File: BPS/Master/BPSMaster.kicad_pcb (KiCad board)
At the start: 2 copper layers, 100 x 75 mm, 160 parts, among them J1 SWD, J10 CurrentSlaveConnector, J11 USB_B_Micro, J12 Conn_01x08, J13 CAN Analyzer, J14 Conn_01x08, J15 Conn_01x02, J2 CarPowerConnector, J3 FrontFans, J4 BackFans, J5 SPI Analyzer, J6 VoltageSlaveConnector, J7 ContactorConnector, J8 CAN_Out, J9 ErrorLightConnector, Q1 VND5N07-E, Q2 NTR4003NT1G, Q3 NTR4003NT1G, Q4 NTR4003NT1G, Q6 BUT11, SW1 B3SL-1002P, SW2 SW_DIP_x01, SW3 SW_Push, U1 STM32F413RHTx, U10 BAS70-04, U11 SI8261ABC-IS, U12 CDSOT23-T24CAN, U13 ADM3055E, U14 SI8261ABC-IS, U15 CP2102N-A01-GQFN24, U2 RI3-1205S, U3 NCP1117-3.3_SOT223, U4 M24128, U5 LTC6256, U6 RN4870-V_RM118, U7 MCP100-315D, U8 LTC6820, U9 HX1188FNL, Y1 8M

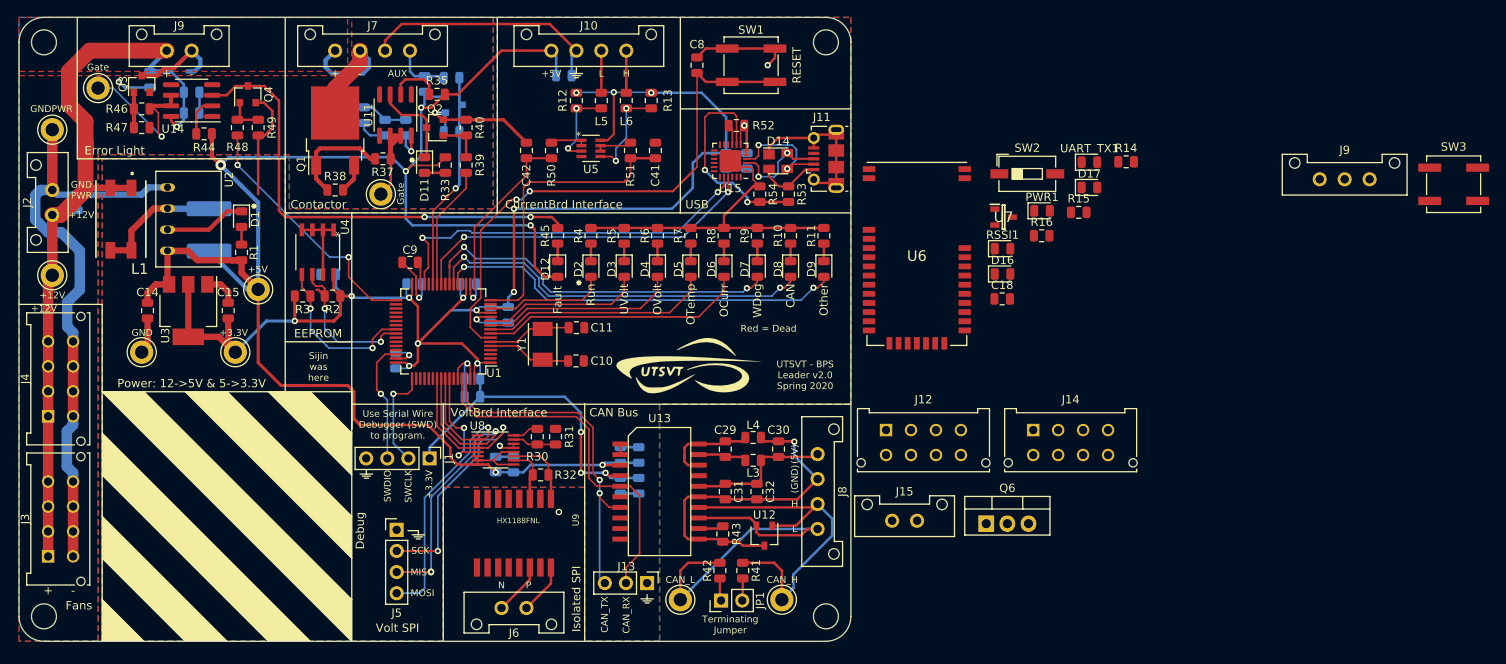
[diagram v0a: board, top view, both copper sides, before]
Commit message: Created new board for Bluetooth module because the antenna cannot have a ground plane on it. Made everything connect using pin headers. Will mount the Bluetooth module board onto the Master board.
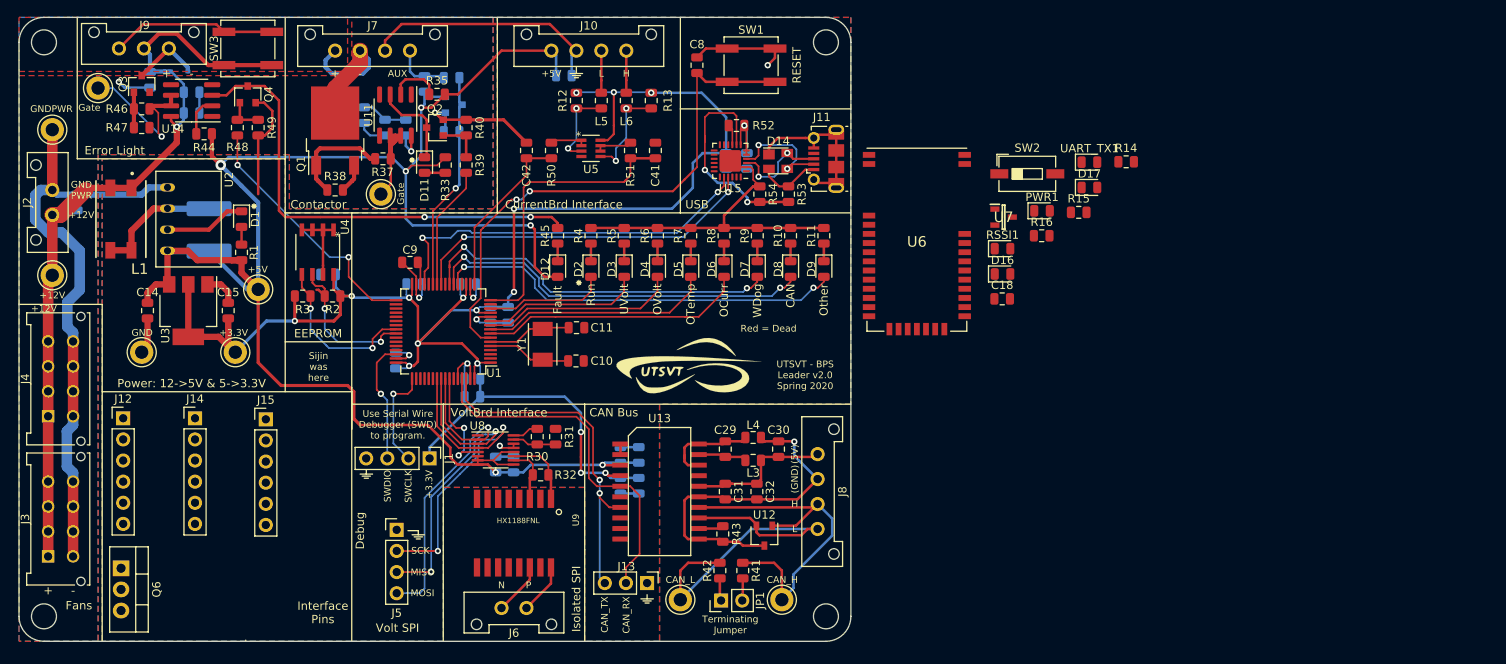
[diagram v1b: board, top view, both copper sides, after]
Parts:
- removed the J9 at (117.8, 79.0)
- J12, J14: value Conn_01x08 -> Conn_01x06; footprint UTSVT_Connectors:Molex_MicroFit3.0_2x4xP3.00mm_PolarizingPeg_Vertical -> Connector_PinHeader_2.54mm:PinHeader_1x06_P2.54mm_Vertical
- J15: value Conn_01x02 -> Conn_01x06; footprint UTSVT_Connectors:Molex_MicroFit3.0_1x2xP3.00mm_PolarizingPeg_Vertical -> Connector_PinHeader_2.54mm:PinHeader_1x06_P2.54mm_Vertical
- moved SW3 145.9 mm to (127.5, 78.7), turned to 180 degrees
- moved J9 145.2 mm to (112.0, 78.7)
- moved Q6 104.1 mm to (112.3, 141.2), turned to 270 degrees
- moved J14 100.8 mm to (121.2, 123.2)
- moved J12 91.7 mm to (112.5, 123.2)
- moved J15 76.3 mm to (129.7, 123.3)
- moved U6 1.71 mm to (207.9, 101.7)
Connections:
- J12 pad 1: /IP7 -> /IP5
- J12 pad 2: /IP6 -> /IP4
- J12 pad 3: /IP5 -> /IP3
- J12 pad 4: /IP4 -> /IP2
- J12 pad 5: /IP3 -> /IP1
- J12 pad 6: /IP2 -> /IP0
- J14 pad 1: /IP15 -> /IP11
- J14 pad 2: /IP14 -> /IP10
- J14 pad 3: /IP13 -> /IP9
- J14 pad 4: /IP12 -> /IP8
- J14 pad 5: /IP11 -> /IP7
- J14 pad 6: /IP10 -> /IP6
- Q6 pad 2: +12V -> GND
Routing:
- net Net-(J9-Pad1): track 0.00 -> 19.9 mm
- net Net-(D13-Pad2): track 11.3 -> 8.32 mm
- net +12V: track 130.9 -> 129.0 mm
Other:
- board text added: "Interface Pins"

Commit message: Finished adding interface pins to master board. For some reason, the mosfet track isn't letting me connect to the fan power. I'm not sure why all these schematics are listed as modified because I didn't change anything in them.
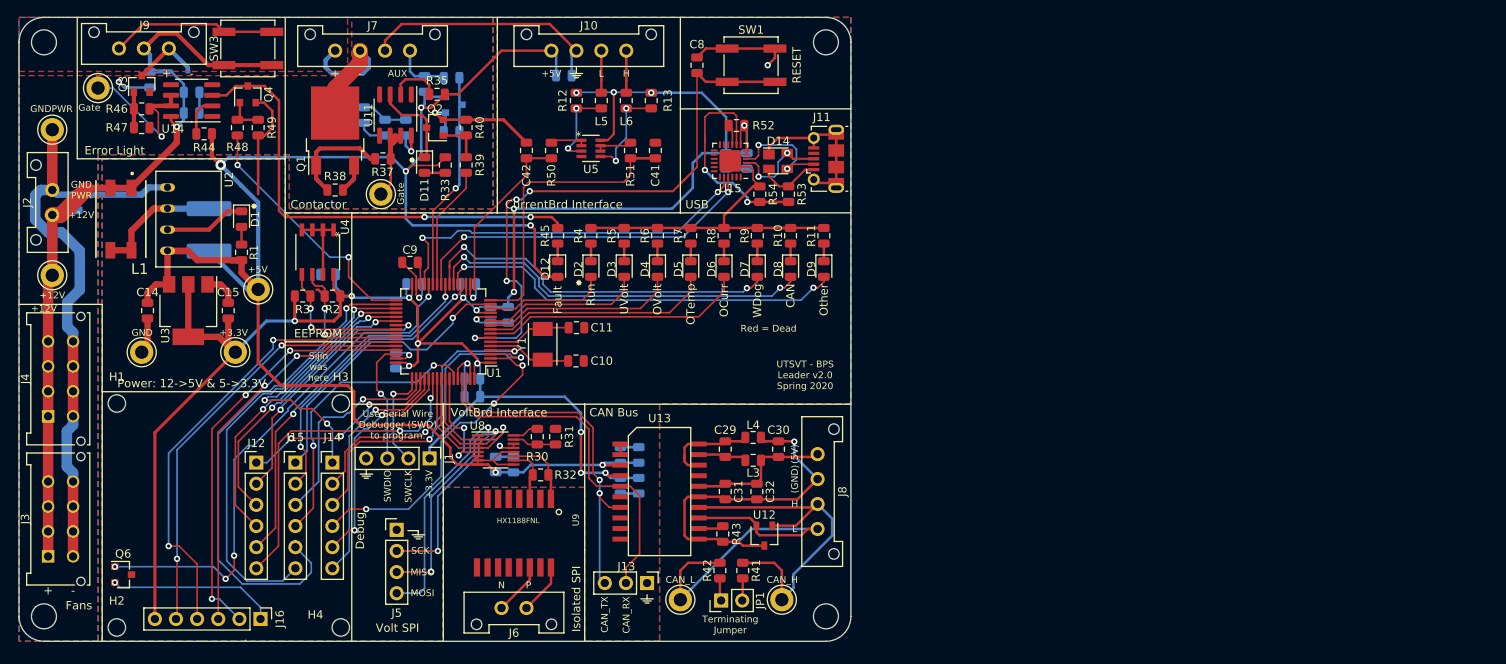
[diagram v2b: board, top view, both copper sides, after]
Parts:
- removed C18: 1uF, Capacitor_SMD:C_0805_2012Metric
- removed D16, D17, PWR1, RSSI1, UART_TX1: LED, LED_SMD:LED_0805_2012Metric
- removed G***: LOGO, UTSVT_Special:Hallock_Image_Small
- removed G***: LOGO, UTSVT_Special:UTSVT_Logo_Symbol
- removed R14: 330, Resistor_SMD:R_0805_2012Metric
- removed R15: 4.7k, Resistor_SMD:R_0805_2012Metric
- removed R16: 10k, Resistor_SMD:R_0805_2012Metric
- removed SW2: SW_DIP_x01, Button_Switch_SMD:SW_DIP_SPSTx01_Slide_6.7x4.1mm_W6.73mm_P2.54mm_LowProfile_JPin
- removed U6: RN4870-V_RM118, UTSVT_BPS:RN4870IRM130
- removed U7: MCP100-315D, UTSVT_BPS:SOT96P240X110-3N
- added H1: MountingHole, MountingHole:MountingHole_2.1mm, F.Cu at (111.8, 121.4)
- added H2: MountingHole, MountingHole:MountingHole_2.1mm, F.Cu at (111.8, 148.3)
- added H3: MountingHole, MountingHole:MountingHole_2.1mm, F.Cu at (138.7, 121.4)
- added H4: MountingHole, MountingHole:MountingHole_2.1mm, F.Cu at (138.7, 148.3)
- added J16: Conn_01x06, Connector_PinHeader_2.54mm:PinHeader_1x06_P2.54mm_Vertical, F.Cu at (129.0, 147.3)
- Q6: footprint Package_TO_SOT_THT:TO-220-3_Vertical -> Package_TO_SOT_SMD:SOT-23
- moved J14 17.4 mm to (137.7, 128.5)
- moved J12 16.9 mm to (128.5, 128.5)
- moved J15 6.31 mm to (133.2, 128.5)
- moved Q6 0.80 mm to (112.5, 142.0), turned to 0 degrees
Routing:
- net /LPTIM1(PWM): track 0.00 -> 63.0 mm, vias 0 -> 4
- net /IP13: track 0.00 -> 60.6 mm, vias 0 -> 1
- net /USART1_TX: track 0.00 -> 55.8 mm, vias 0 -> 2
- net /IP12: track 0.00 -> 52.6 mm, vias 0 -> 1
- net /USART1_RX: track 0.00 -> 52.1 mm, vias 0 -> 2
- net /USART1_CTS: track 0.00 -> 51.0 mm, vias 0 -> 3
- net /USART1_RTS: track 0.00 -> 47.9 mm, vias 0 -> 2
- net /IP1: track 0.00 -> 44.0 mm, vias 0 -> 2
- net /IP9: track 0.00 -> 40.6 mm, vias 0 -> 2
- net /IP0: track 0.00 -> 40.5 mm, vias 0 -> 2
- net /IP8: track 0.00 -> 38.2 mm, vias 0 -> 3
- net /IP2: track 0.00 -> 37.0 mm, vias 0 -> 2
- net /IP10: track 0.00 -> 36.2 mm, vias 0 -> 2
- net /IP16: track 0.00 -> 35.9 mm, vias 0 -> 2
- net /IP17: track 0.00 -> 35.7 mm, vias 0 -> 1
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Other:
- board text removed: "Interface Pins"

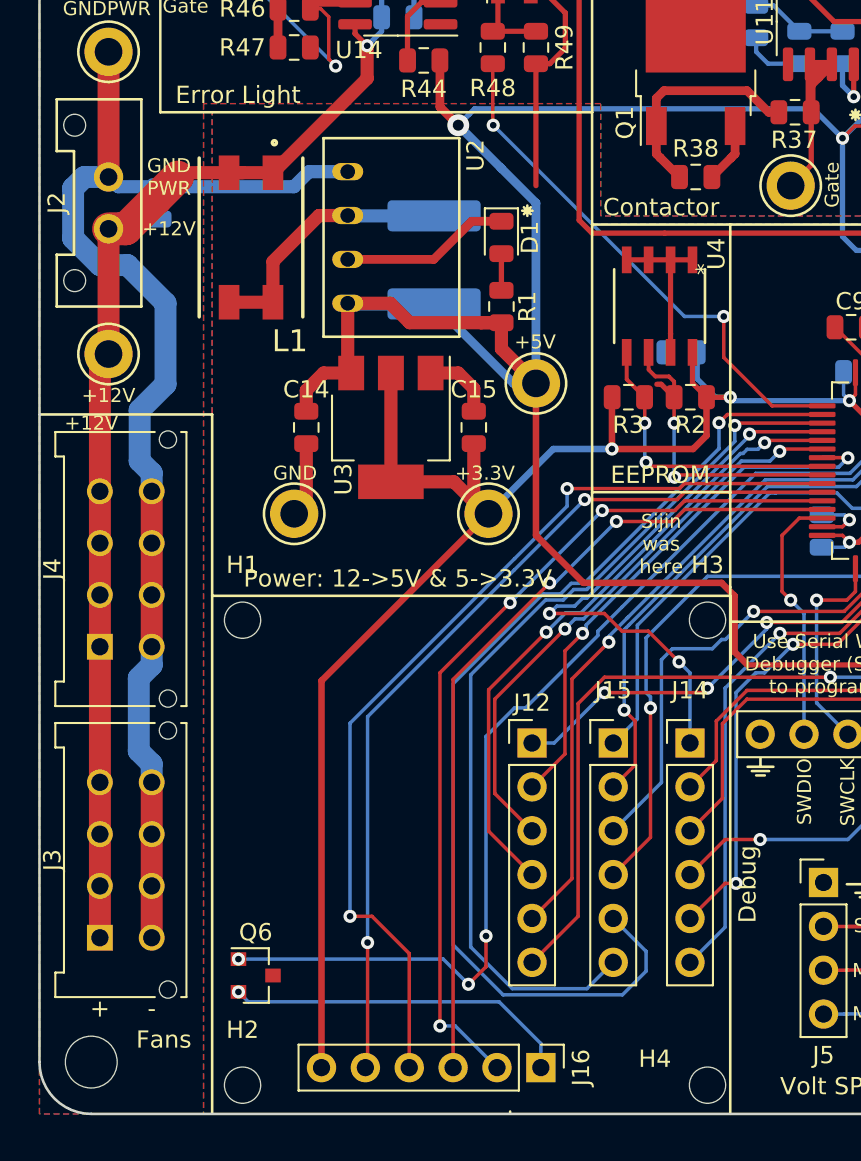
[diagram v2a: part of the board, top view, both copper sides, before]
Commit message: Finished master board. Working to make sure that bluetooth mount won't cover anything important on master board, yet still be big enough to hold everything.
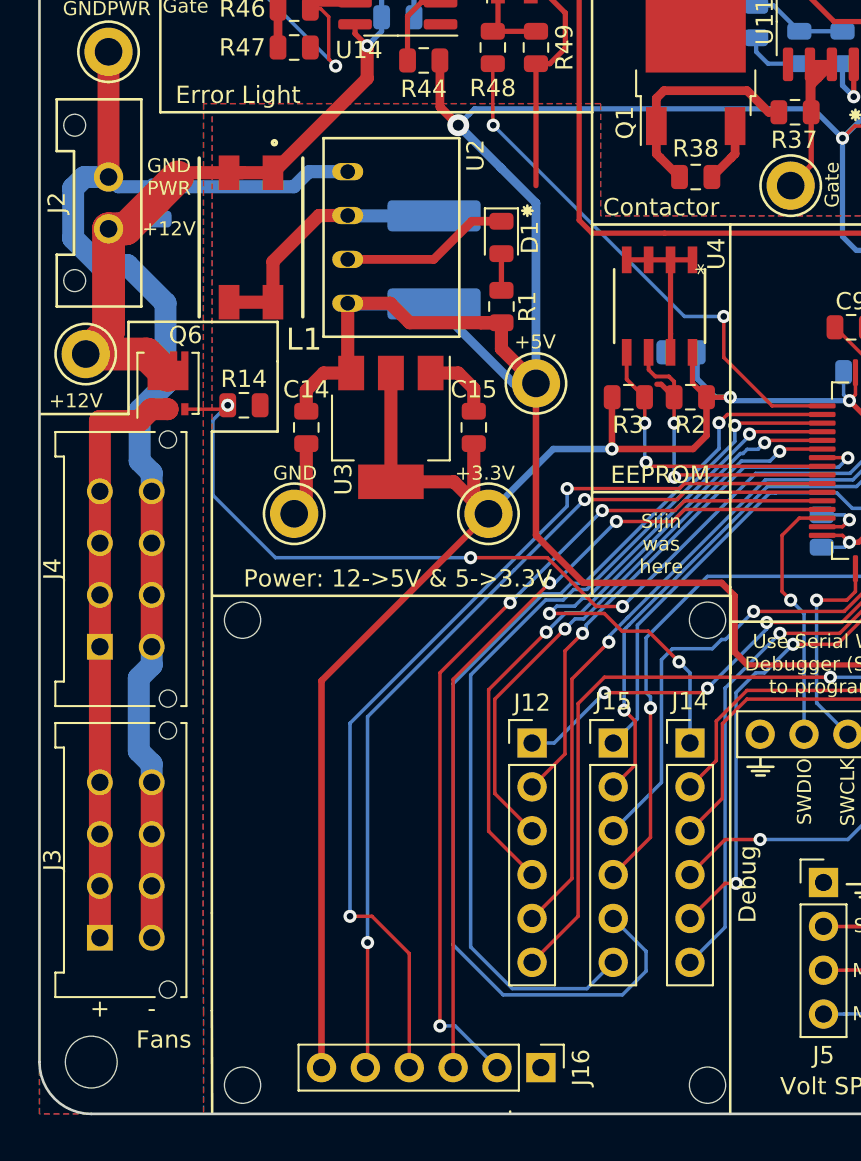
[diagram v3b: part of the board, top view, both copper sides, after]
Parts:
- added R14: 10k, Resistor_SMD:R_0805_2012Metric, F.Cu at (111.8, 109.0)
- Q6: value BUT11 -> DMP3013SFV; footprint Package_TO_SOT_SMD:SOT-23 -> Package_SON:Diodes_PowerDI3333-8
- moved Q6 34.7 mm to (107.4, 107.7), turned to 90 degrees
- moved TP1 1.32 mm to (102.7, 106.0)
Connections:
- Q6 pad 1: /LPTIM1(PWM) -> Net-(J3-Pad1)
- Q6 pad 2: GND -> Net-(J3-Pad1)
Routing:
- net Net-(J3-Pad1): track 0.00 -> 42.0 mm
- net +12V: track 129.0 -> 93.8 mm
- net GND: track 220.5 -> 200.4 mm, vias 9 -> 8
- net /LPTIM1(PWM): track 63.0 -> 57.7 mm

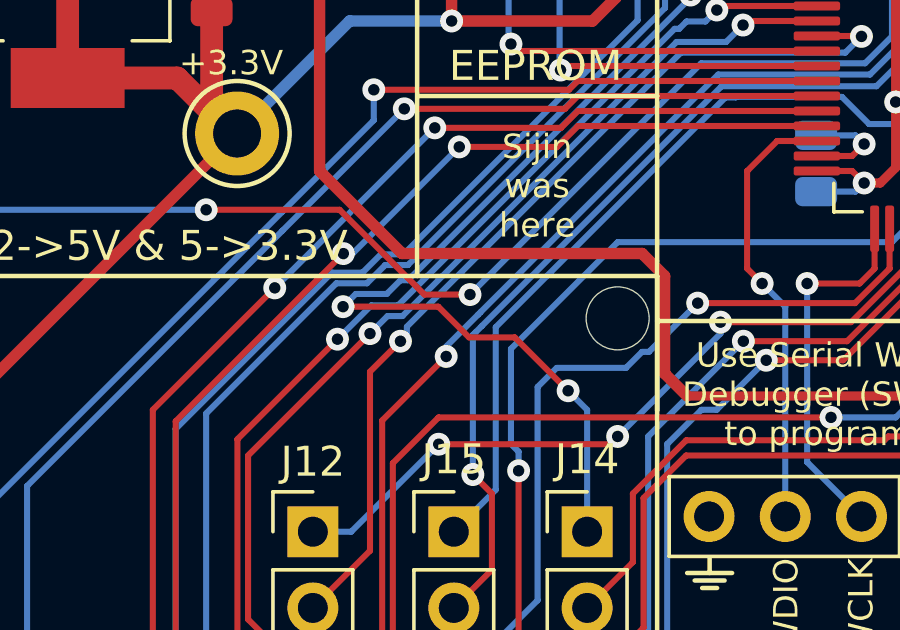
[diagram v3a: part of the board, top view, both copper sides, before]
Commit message: Added signature
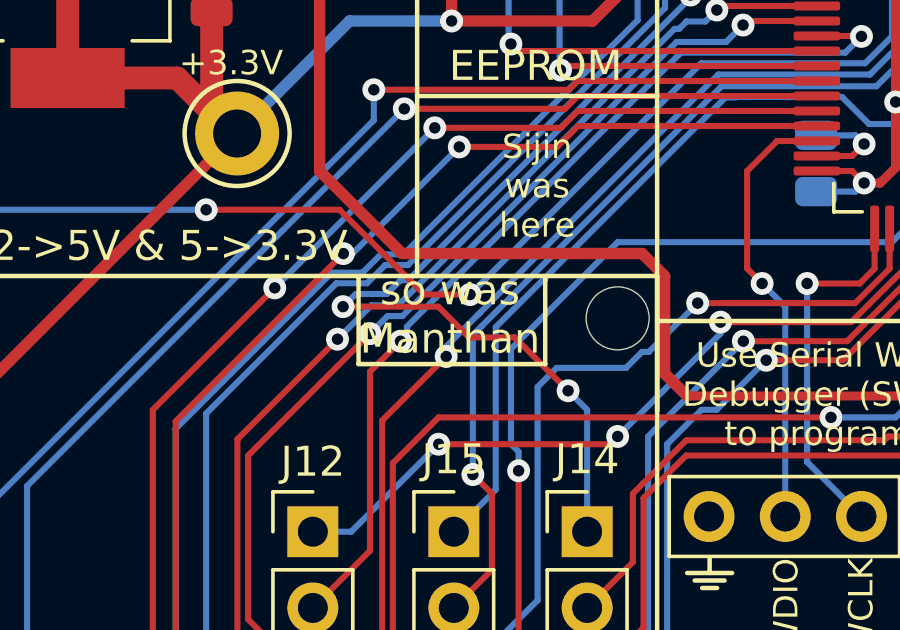
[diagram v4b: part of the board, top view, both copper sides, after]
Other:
- board text added: "so was Manthan"
